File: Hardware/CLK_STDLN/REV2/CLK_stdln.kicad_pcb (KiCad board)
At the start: 2 copper layers, 63.9 x 67 mm, 43 parts, among them J1 Conn_01x04_Male, J2 Conn_Coaxial, J3 Conn_01x02, J4 Conn_02x20_Counter_Clockwise, Q1 BC547, Q2 BC547, Q3 BC547, SW1 SW_Push, SW2 SW_SPDT, SW3 SW_SPDT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

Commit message: 0041 | 0,1h | review STDLN CLK REV 2
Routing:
- net Net-(R6-Pad2): track 16.5 -> 15.3 mm
- net Net-(C7-Pad1): track 14.3 -> 13.2 mm
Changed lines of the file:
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@@
     (thickness 1.6)
     (drawings 5)
-    (tracks 318)
+    (tracks 321)
     (modules 43)
     (nets 69)
@@
   )
   (gr_rect (start 209.31 153.54) (end 145.36 86.52) (layer "Edge.Cuts") (width 0.05))
+  (segment (start 204.952 134.864) (end 204.894 134.864) (width 0.2) (layer "F.Cu") (net 5))
+  (segment (start 204.894 134.864) (end 203.122 133.092) (width 0.2) (layer "F.Cu") (net 5))
+  (segment (start 203.122 133.092) (end 203.122 129.574) (width 0.2) (layer "F.Cu") (net 5))
+  (segment (start 174.4325 123.72) (end 174.4325 130.20776) (width 0.2) (layer "F.Cu") (net 52))
+  (segment (start 174.4325 130.20776) (end 175.68112 131.45638) (width 0.2) (layer "F.Cu") (net 52))
+  (segment (start 175.68112 133.77112) (end 175.68112 131.45638) (width 0.2) (layer "F.Cu") (net 52))
+  (segment (start 175.68112 131.45638) (end 177.3825 129.755) (width 0.2) (layer "F.Cu") (net 52))
+  (segment (start 203.88 105.78) (end 200.075 101.975) (width 0.2) (layer "F.Cu") (net 4))
+  (segment (start 200.075 101.975) (end 199.95 101.85) (width 0.2) (layer "F.Cu") (net 4))
+  (segment (start 194.9 103.24) (end 198.12 100.02) (width 0.2) (layer "F.Cu") (net 4))
+  (segment (start 200.075 101.975) (end 198.12 100.02) (width 0.2) (layer "F.Cu") (net 4))
+  (segment (start 198.12 100.02) (end 199.95 98.19) (width 0.2) (layer "F.Cu") (net 4))
+  (segment (start 199.95 98.19) (end 199.95 97.13) (width 0.2) (layer "F.Cu") (net 4))
+  (segment (start 205.06 105.78) (end 203.88 105.78) (width 0.2) (layer "F.Cu") (net 4))
+  (segment (start 186.99699 99.59299) (end 186.99699 97.74301) (width 1) (layer "B.Cu") (net 2))
+  (segment (start 185.65699 97.74301) (end 185.402 97.998) (width 1) (layer "B.Cu") (net 2))
+  (segment (start 186.99699 97.74301) (end 186.99699 96.55301) (width 1) (layer "B.Cu") (net 2))
+  (segment (start 186.99699 97.74301) (end 185.65699 97.74301) (width 1) (layer "B.Cu") (net 2))
+  (segment (start 186.99699 96.55301) (end 187.49 96.06) (width 1) (layer "B.Cu") (net 2))
   (segment (start 168.432 96.59) (end 157.55 96.59) (width 0.2) (layer "F.Cu") (net 41))
   (segment (start 169.64 97.798) (end 168.432 96.59) (width 0.2) (layer "F.Cu") (net 41))
@@
   (segment (start 179.9075 131.805) (end 184.135 131.805) (width 1) (layer "B.Cu") (net 2))
   (segment (start 187.35 135.02) (end 187.35 140.42) (width 1) (layer "B.Cu") (net 2))
-  (segment (start 175.6925 132.36) (end 175.68112 133.77112) (width 0.2) (layer "F.Cu") (net 52))
   (segment (start 172.34 93.45) (end 171.29 94.5) (width 0.2) (layer "F.Cu") (net 56))
   (segment (start 185.8 93.45) (end 172.34 93.45) (width 0.2) (layer "F.Cu") (net 56))
@@
   (segment (start 189.719 113.501) (end 194.9 108.32) (width 1) (layer "F.Cu") (net 2))
   (segment (start 188.33 113.501) (end 189.719 113.501) (width 1) (layer "F.Cu") (net 2))
-  (segment (start 175.7025 132.36) (end 175.7025 131.9075) (width 0.25) (layer "F.Cu") (net 52))
-  (segment (start 175.47625 132.14375) (end 174.4325 131.1) (width 0.25) (layer "F.Cu") (net 52))
-  (segment (start 175.7025 131.9075) (end 175.7025 131.435) (width 0.25) (layer "F.Cu") (net 52))
-  (segment (start 175.47625 132.13375) (end 175.7025 131.9075) (width 0.2) (layer "F.Cu") (net 52))
-  (segment (start 175.6925 132.36) (end 175.47625 132.14375) (width 0.25) (layer "F.Cu") (net 52))
-  (segment (start 175.47625 132.14375) (end 175.47625 132.13375) (width 0.2) (layer "F.Cu") (net 52))
   (segment (start 174.4325 123.72) (end 175.9825 122.17) (width 0.25) (layer "F.Cu") (net 52))
-  (segment (start 175.7025 131.435) (end 177.3825 129.755) (width 0.25) (layer "F.Cu") (net 52))
-  (segment (start 175.7025 132.36) (end 175.6925 132.36) (width 0.25) (layer "F.Cu") (net 52))
-  (segment (start 174.4325 131.1) (end 174.4325 123.72) (width 0.25) (layer "F.Cu") (net 52))
   (segment (start 194.9 105.78) (end 194.9 105.85) (width 0.2) (layer "B.Cu") (net 66))
   (segment (start 169.64 116.04) (end 172.179 113.501) (width 1) (layer "F.Cu") (net 2))
@@
   (segment (start 172.55 131.704502) (end 172.55 129.16) (width 0.2) (layer "F.Cu") (net 61))
   (segment (start 172.55 129.16) (end 169.64 126.25) (width 0.2) (layer "F.Cu") (net 61))
-  (segment (start 185.552 97.998) (end 187.49 96.06) (width 1) (layer "B.Cu") (net 2))
   (segment (start 185.402 97.998) (end 185.552 97.998) (width 1) (layer "B.Cu") (net 2))
   (segment (start 187.49 96.06) (end 189.21 96.06) (width 1) (layer "B.Cu") (net 2))
@@
   (segment (start 186.99699 112.16799) (end 186.99699 105.20901) (width 1) (layer "B.Cu") (net 2))
   (segment (start 188.33 113.501) (end 186.99699 112.16799) (width 1) (layer "B.Cu") (net 2))
-  (segment (start 186.99699 99.59299) (end 185.402 97.998) (width 1) (layer "B.Cu") (net 2))
   (via (at 188.33 113.501) (size 0.8) (drill 0.4) (layers "F.Cu" "B.Cu") (net 2))
   (segment (start 173.16 107.531) (end 172.755 107.531) (width 0.2) (layer "F.Cu") (net 53))
@@
   (segment (start 204.952 134.864) (end 204.952 137.404) (width 0.2) (layer "F.Cu") (net 5))
   (segment (start 199.822 129.574) (end 199.822 129.734) (width 0.2) (layer "F.Cu") (net 5))
-  (segment (start 199.822 129.734) (end 204.952 134.864) (width 0.2) (layer "F.Cu") (net 5))
   (segment (start 204.932 134.864) (end 204.952 134.864) (width 0.2) (layer "B.Cu") (net 5))
   (segment (start 199.822 129.574) (end 203.122 129.574) (width 0.2) (layer "F.Cu") (net 5))
@@
   (segment (start 182.1725 129.755) (end 179.6575 127.24) (width 0.2) (layer "F.Cu") (net 54))
   (segment (start 175.9925 127.24) (end 175.9825 127.25) (width 0.2) (layer "F.Cu") (net 54))
-  (segment (start 194.92 103.24) (end 199.95 98.21) (width 0.2) (layer "F.Cu") (net 4))
   (segment (start 194.9 103.24) (end 194.92 103.24) (width 0.2) (layer "F.Cu") (net 4))
   (segment (start 199.95 98.21) (end 199.95 97.13) (width 0.2) (layer "F.Cu") (net 4))
-  (segment (start 204.92 105.64) (end 197.3 105.64) (width 0.2) (layer "F.Cu") (net 4))
   (segment (start 205.06 105.78) (end 204.92 105.64) (width 0.2) (layer "F.Cu") (net 4))
-  (segment (start 197.3 105.64) (end 194.9 103.24) (width 0.2) (layer "F.Cu") (net 4))
   (segment (start 183.3625 133.18) (end 183.3625 130.945) (width 0.2) (layer "F.Cu") (net 54))
   (segment (start 182.4125 134.13) (end 183.3625 133.18) (width 0.2) (layer "F.Cu") (net 54))

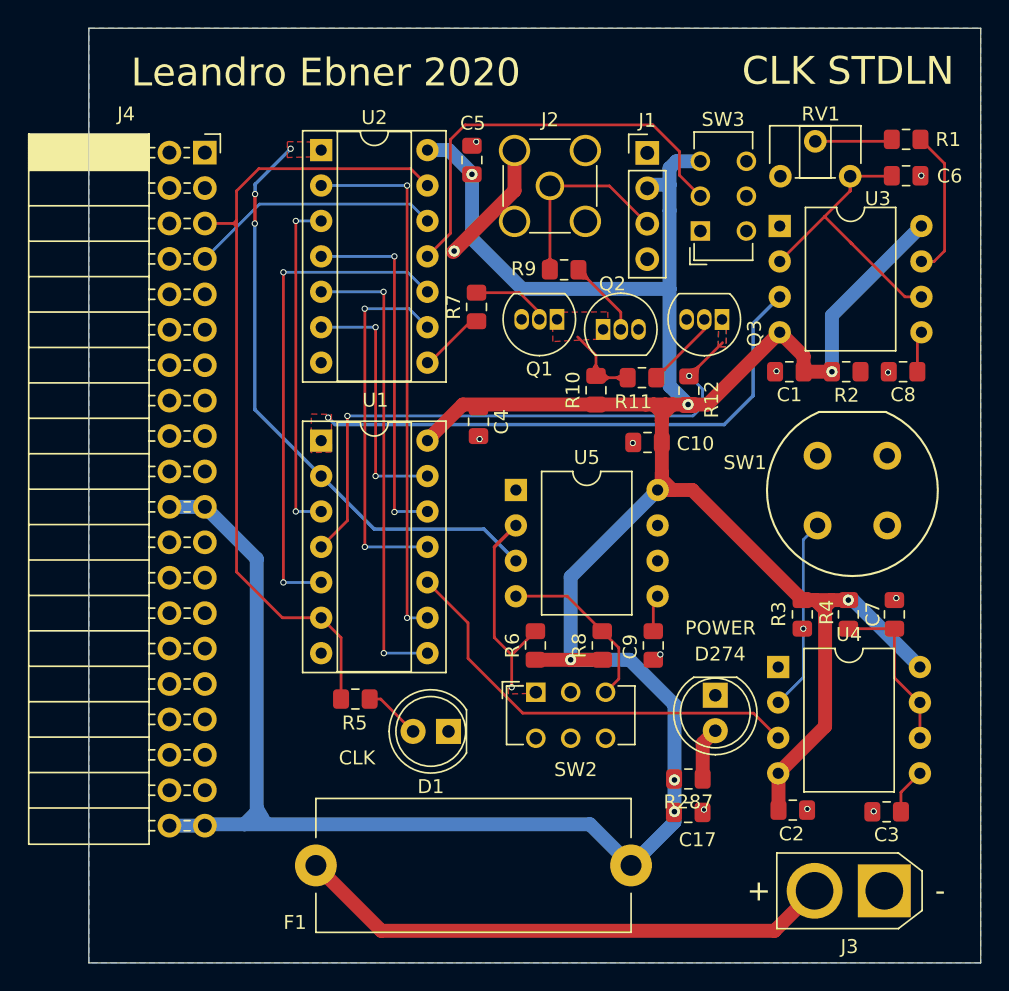
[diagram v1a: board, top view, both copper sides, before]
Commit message: quickfix CLK_STDLN
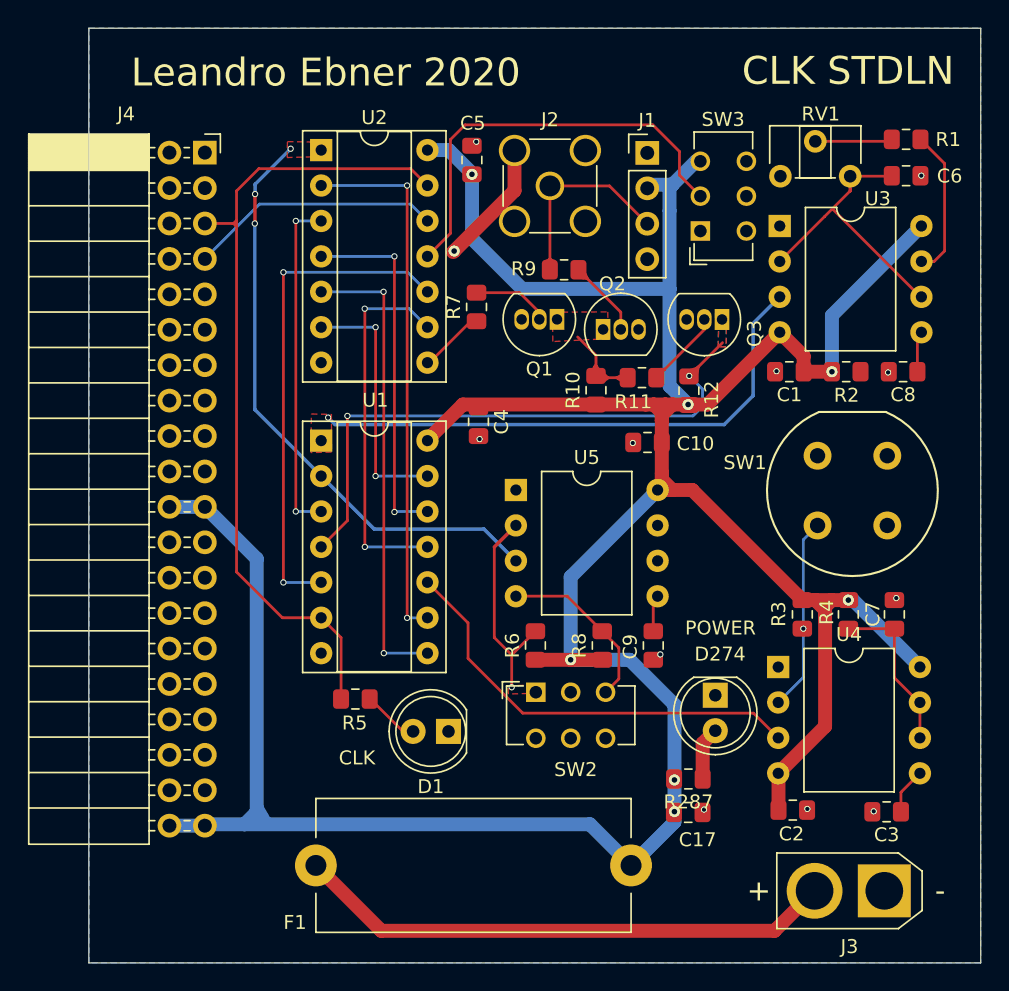
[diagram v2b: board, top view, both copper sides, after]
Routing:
- net +5V: track 250.2 -> 249.5 mm
- net Net-(C6-Pad1): track 22.0 -> 21.5 mm

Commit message: 0047 | 0.5h | review ALU Module
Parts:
- C1, C10, C17, C2, C3, C4, C5, C6, C7, C8, C9: footprint Capacitor_SMD:C_0805_2012Metric_Pad1.15x1.40mm_HandSolder -> Capacitor_SMD:C_0805_2012Metric
- R1, R10, R11, R12, R2, R287, R3, R4, R5, R6, R7, R8, R9: footprint Resistor_SMD:R_0805_2012Metric_Pad1.15x1.40mm_HandSolder -> Resistor_SMD:R_0805_2012Metric
